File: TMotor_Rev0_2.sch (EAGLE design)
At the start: 77 parts, among them J1 5015680507, J10 5015680207, J2 5015680507, J7 5015680207, J8 5015680207, J9 5015680207, U1 INA125U, U2 INA125U, U3 INA125U, U4 INA125U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

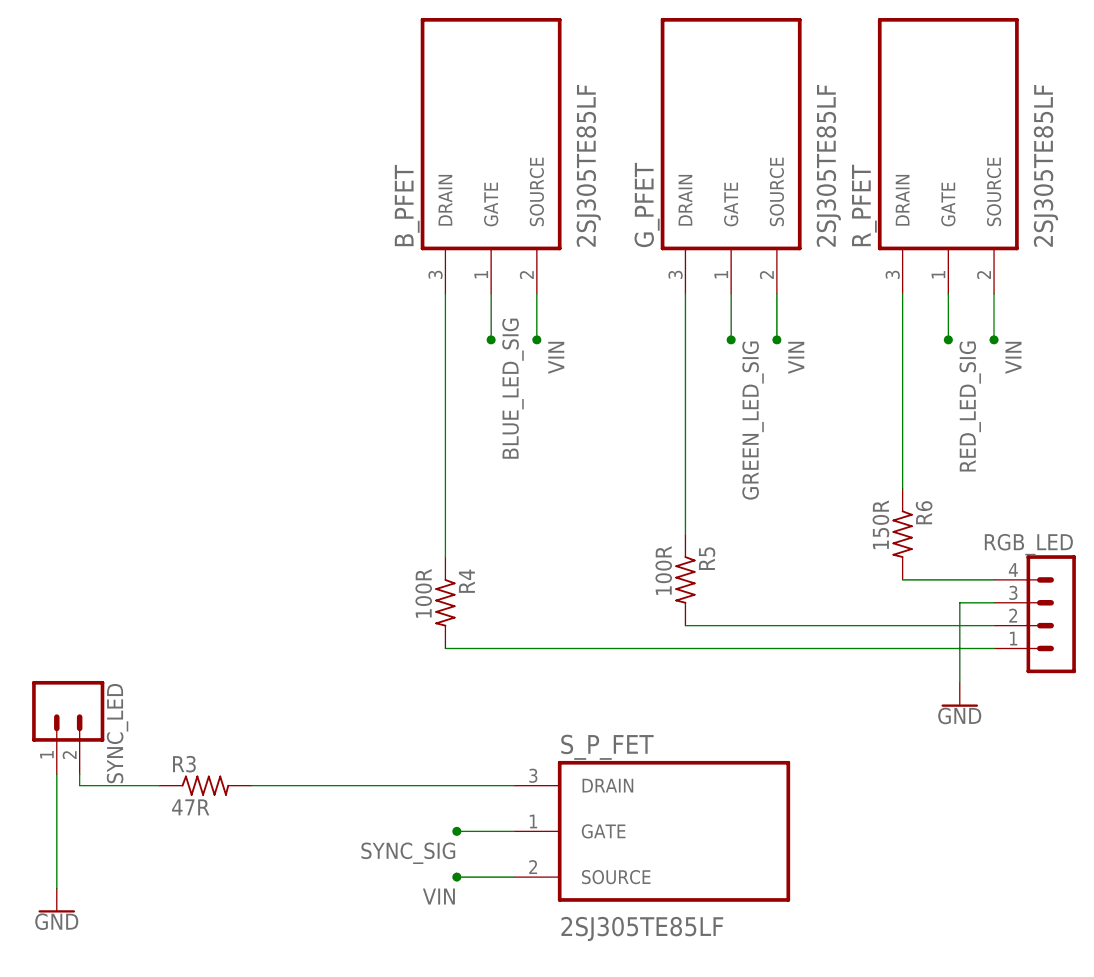
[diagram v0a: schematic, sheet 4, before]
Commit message: updated LED power
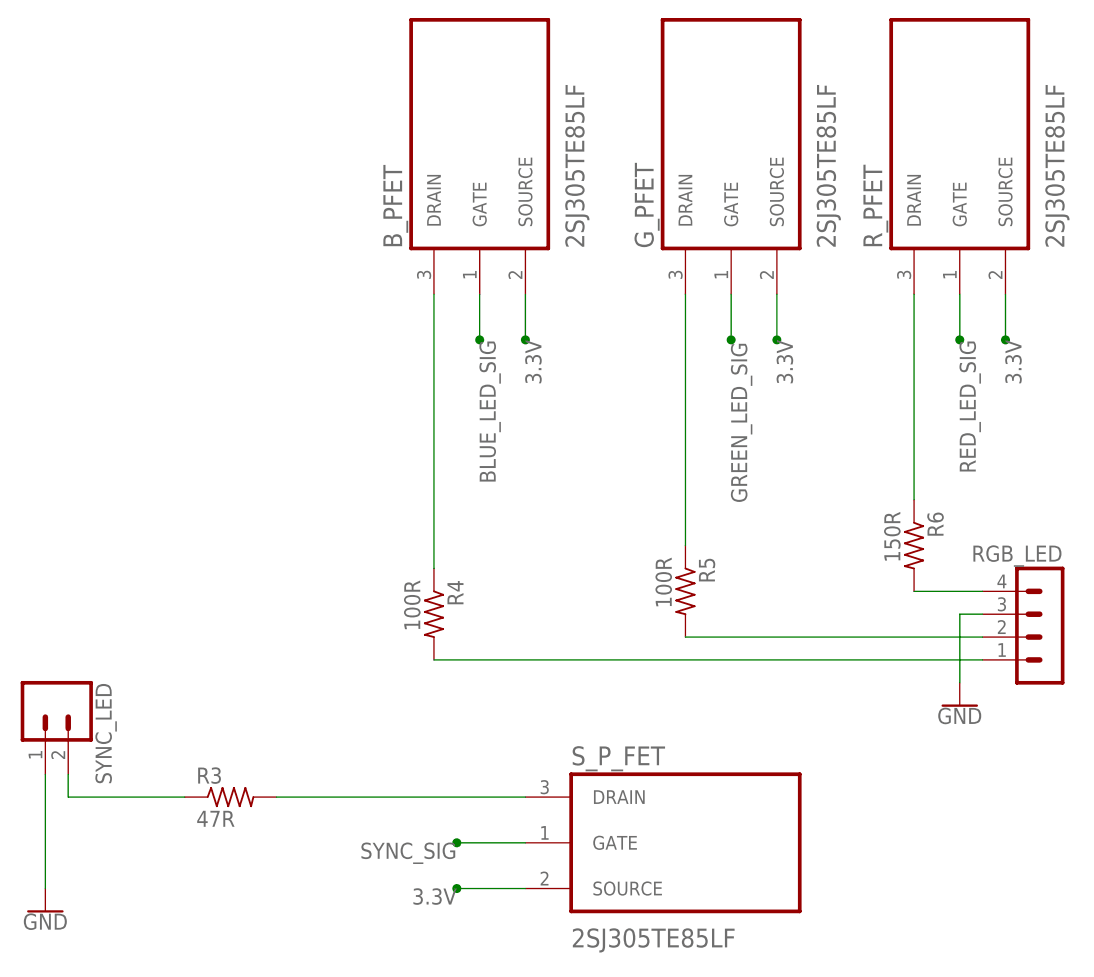
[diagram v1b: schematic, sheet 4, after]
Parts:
- added C23: 100nF, rcl:C-EU050-024X044
- C3, C5, C9: value 0.1uF -> 100nF
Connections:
- new net N$14: U4.VREF5
- new net N$19: U4.VREF2.5
- new net N$20: U2.VREF10
- new net N$21: U2.VREF5
- new net N$22: U2.VREF2.5
- new net N$37: U1.VREF10
- new net N$38: U1.VREF5
- new net N$39: U1.VREF2.5
- new net N$4: U4.VREF10
- new net N$40: U3.VREF10
- new net N$41: U3.VREF5
- new net N$42: U3.VREF2.5
- net 3.3V: now also B_PFET.SOURCE, G_PFET.SOURCE, R_PFET.SOURCE, S_P_FET.SOURCE
- net GND: now also C23.1
- net MISO: now also U$1.11/MOSI; no longer U$1.12/MISO
- net MOSI: now also U$1.12/MISO; no longer U$1.11/MOSI
- net VIN: now also C23.2; no longer B_PFET.SOURCE, G_PFET.SOURCE, R_PFET.SOURCE, S_P_FET.SOURCE
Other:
- moved on the sheet: B_PFET, R3, R4, R5, R6, RGB_LED, R_PFET, SYNC_LED, S_P_FET
